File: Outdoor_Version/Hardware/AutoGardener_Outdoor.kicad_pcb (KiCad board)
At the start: 2 copper layers, 22 x 30 mm, 25 parts, among them J1 SWO, J2 Header_1x3, J3 Header_1x3, J4 Header_1x2, Q1 FDN308P, Q2 IRLML6346TRPBF, U1 STM32L031K6T6, U2 AP2204RB-3.3TRG1

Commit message: Started a new kicad project.
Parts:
- moved R2 7.25 mm to (222.0, 100.0), turned to 0 degrees
- moved LD13 4.78 mm to (226.0, 100.0), turned to 180 degrees
- moved SB2 3.06 mm to (225.8, 85.6)
- moved BAT1 3.00 mm to (217.0, 109.0), turned to 270 degrees
- moved C3 2.46 mm to (227.0, 97.0)
- moved LD3 1.82 mm to (226.0, 104.0), turned to 180 degrees
- moved C1 1.26 mm to (215.6, 89.2), turned to 180 degrees
- moved R3 1.12 mm to (222.0, 102.0)
- moved Q2 0.79 mm to (222.0, 105.0)
- moved C2 0.72 mm to (215.6, 92.4), turned to 180 degrees
- moved SB1 0.15 mm to (219.5, 85.6)
- turned C4 to 180 degrees
- turned C5 to 180 degrees
- turned C6 to 180 degrees
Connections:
- J2 pad 1: /UART_TX -> /UART_RX
- J2 pad 2: /UART_RX -> /UART_TX
- U1 pad 10: Net-(U1-Pad10) -> /BAT_LO
- U1 pad 15: /SENS_ENA -> Net-(U1-Pad15)
- U1 pad 18: /BAT_LO -> Net-(U1-Pad18)
- U1 pad 25: Net-(U1-Pad25) -> /SENS_ENA
- U1 pad 27: /OUT1 -> Net-(U1-Pad27)
- U1 pad 9: Net-(U1-Pad9) -> /OUT1
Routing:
- net VCC: track 0.00 -> 51.5 mm, vias 0 -> 3
- net /NRST: track 0.00 -> 23.4 mm, vias 0 -> 2
- net /UART_TX: track 0.00 -> 16.7 mm
- net /UART_RX: track 0.00 -> 15.1 mm
- net /ADC_SOIL1: track 0.00 -> 13.9 mm, vias 0 -> 1
- net /SENS_ENA: track 0.00 -> 12.7 mm, vias 0 -> 2
- net +5V: track 0.00 -> 11.5 mm
- net /SWDIO: track 0.00 -> 10.2 mm
- net /OUT1: track 0.00 -> 9.30 mm
- net /SWCLK: track 0.00 -> 6.29 mm
- net VDDA: track 0.00 -> 5.85 mm
- net /BAT_LO: track 0.00 -> 4.12 mm
- net Net-(J4-Pad2): track 0.00 -> 4.12 mm
- net Net-(LD3-Pad2): track 0.00 -> 3.62 mm
- net GND: track 0.00 -> 2.88 mm, vias 0 -> 23
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- added copper zone on F.Cu, net GND
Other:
- board text added: "+"
- board text added: "-"
- board text added: "AUTOGARDENER OUTDOOR v1"
- board text added: "BAT"
- board text added: "G"
- board text added: "RX TX GND"
- board text added: "S"
- board text added: "SOIL SENSOR"
- board text added: "SWO"
- board text added: "UART"
- board text added: "V"
- board text added: "VALVE"

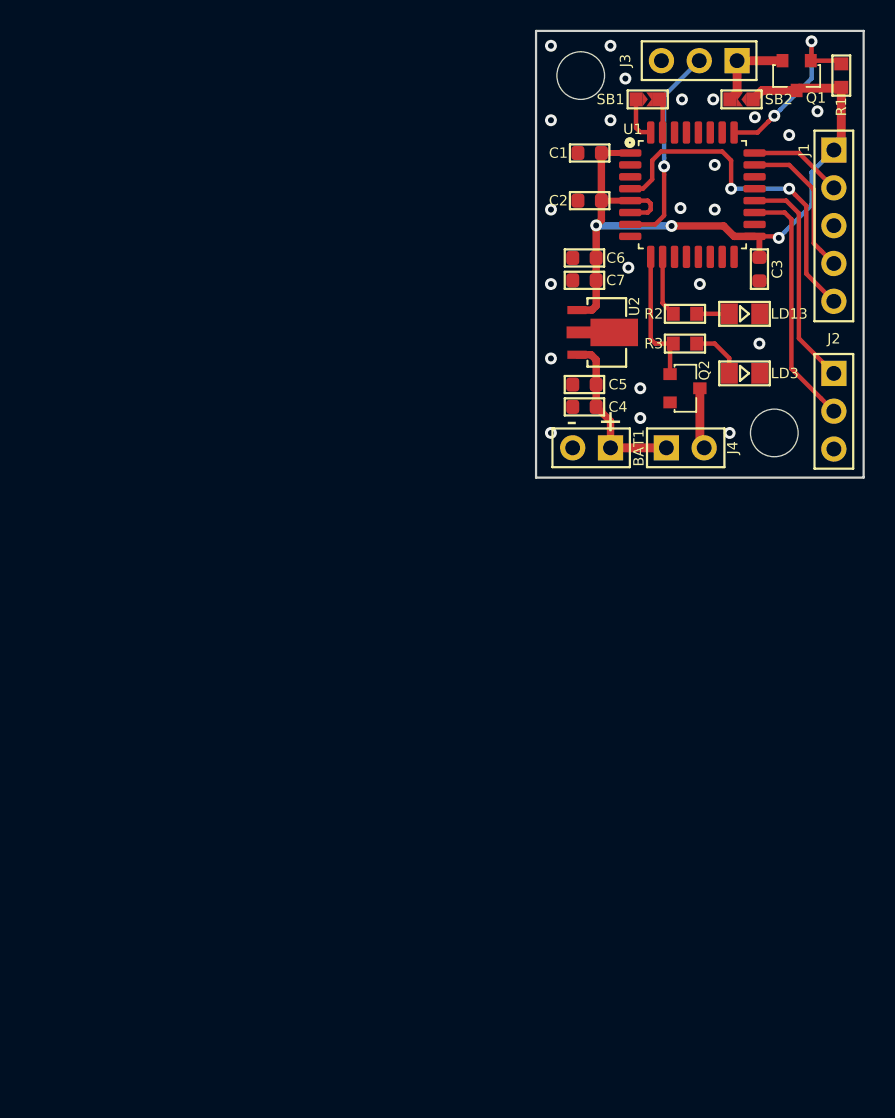
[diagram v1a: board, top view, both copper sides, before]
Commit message: Finished the design of the outdoor version of the gardener. Generated Gerbers.
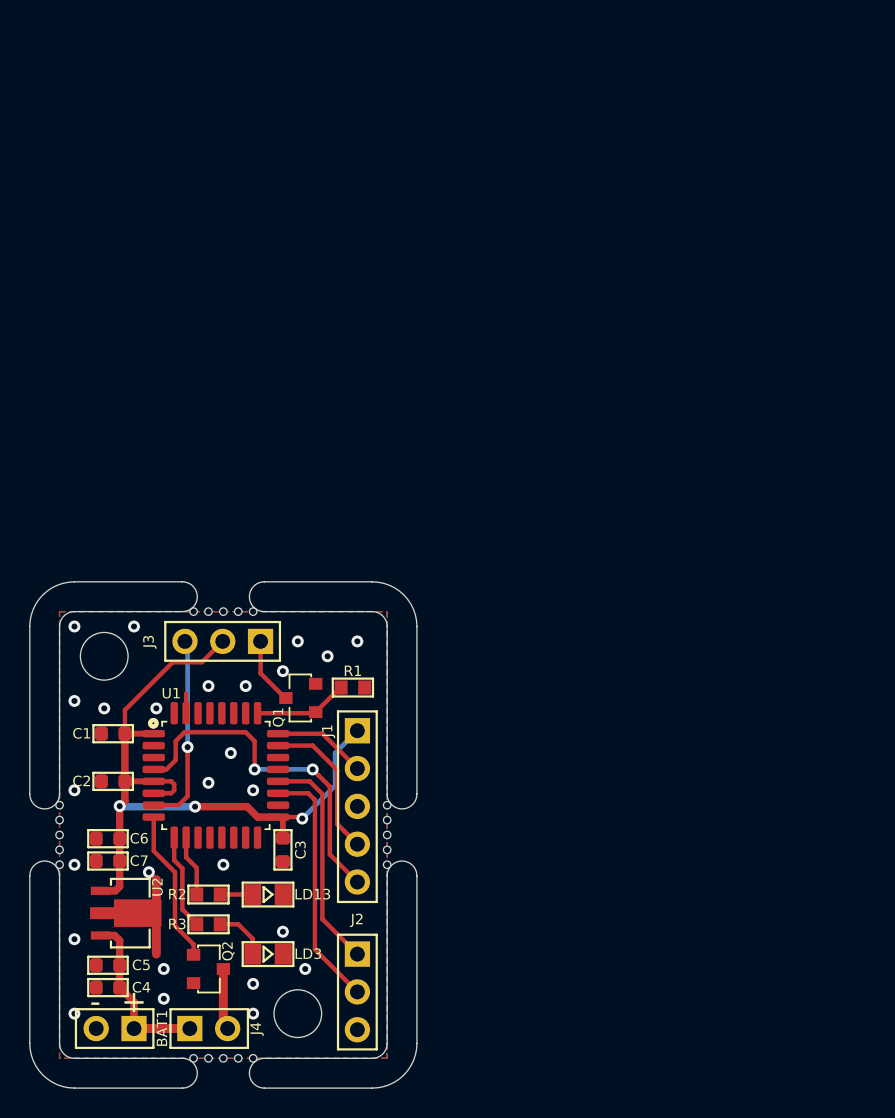
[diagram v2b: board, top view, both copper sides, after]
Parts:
- removed SB1, SB2: SolderBridge, MRS_Connectors:SB0603
- added H111: Mr_Gardener_Logo_Small, Logos:mrg_gardener_08mm, B.Cu at (195.0, 139.0)
- added H3: Break_away_tab, MRS_Mechanical:Breakaway_tab_holes, F.Cu at (191.0, 120.0)
- added H4: Break_away_tab, MRS_Mechanical:Breakaway_tab_holes, F.Cu at (191.0, 150.0)
- added H5: Break_away_tab, MRS_Mechanical:Breakaway_tab_holes, F.Cu at (202.0, 135.0)
- added H6: Break_away_tab, MRS_Mechanical:Breakaway_tab_holes, F.Cu at (180.0, 135.0)
- Q1: value FDN308P -> 2N7002P.215
- Q2: value IRLML6346TRPBF -> 2N7002P.215
- moved Q1 53.4 mm to (196.2, 125.8), turned to 180 degrees
- moved R1 52.6 mm to (199.7, 125.1), turned to 0 degrees
- moved BAT1 50.4 mm to (185.0, 148.0)
- moved C2 50.4 mm to (183.6, 131.4)
- moved C3 50.4 mm to (195.0, 136.0)
- moved C4 50.4 mm to (183.2, 145.2)
- moved C5 50.4 mm to (183.2, 143.8)
- moved C6 50.4 mm to (183.2, 135.2)
- moved C7 50.4 mm to (183.2, 136.8)
- moved H1 50.4 mm to (183.0, 123.0)
- moved H2 50.4 mm to (196.0, 147.0)
- moved J1 50.4 mm to (200.0, 128.0)
- moved J2 50.4 mm to (200.0, 143.0)
- moved J3 50.4 mm to (193.5, 122.0)
- moved J4 50.4 mm to (188.8, 148.0)
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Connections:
- J3 pad 1: VDDA -> Net-(J3-Pad1)
- J3 pad 2: /ADC_SOIL1 -> VCC
- J3 pad 3: GND -> /ADC_SOIL1
- Q1 pad 2: VDDA -> GND
- Q1 pad 3: VCC -> Net-(J3-Pad1)
- R1 pad 1: VCC -> /SENS_ENA
- R1 pad 2: /SENS_ENA -> GND
- R3 pad 1: /OUT1 -> /LED1
- U1 pad 31: Net-(SB1-Pad2) -> GND
- U1 pad 8: Net-(U1-Pad8) -> /OUT1
- U1 pad 9: /OUT1 -> /LED1
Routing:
- net /LED1: track 0.00 -> 6.75 mm
- net /SENS_ENA: track 12.7 -> 6.33 mm, vias 2 -> 0
- net VDDA: track 5.85 -> 0.00 mm
- net GND: track 2.88 -> 8.11 mm, vias 23 -> 26
- net Net-(J3-Pad1): track 0.00 -> 4.53 mm
- net Net-(SB1-Pad2): track 2.16 -> 0.00 mm
- net /OUT1: track 9.30 -> 10.4 mm
- net /ADC_SOIL1: track 13.9 -> 13.0 mm
- net VCC: track 51.5 -> 50.9 mm
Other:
- board size 22 x 30 mm -> 26 x 34 mm
- board text added: "A"
- board text added: "Mr. Gardener Jr."
- board text added: "rev 1"
- board text removed: "AUTOGARDENER OUTDOOR v1"
- board text removed: "S"

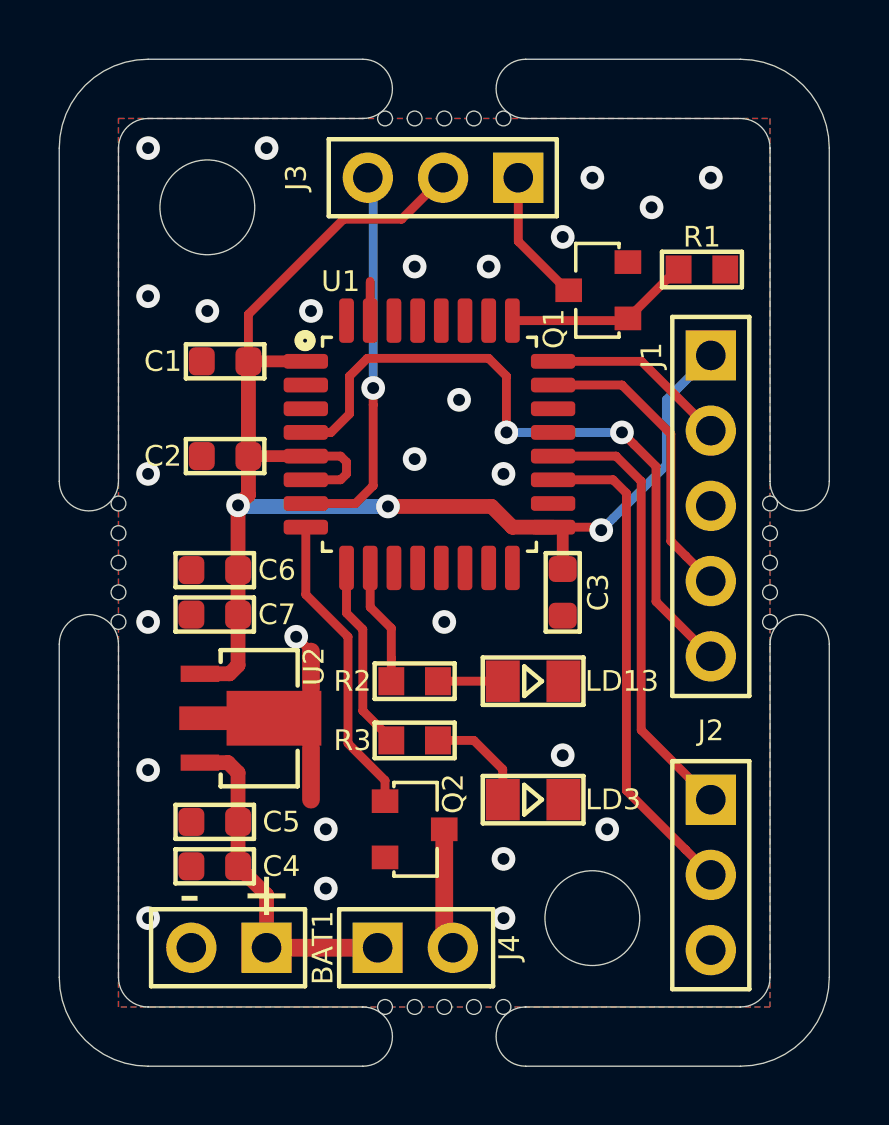
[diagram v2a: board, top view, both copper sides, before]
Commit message: Added some mechanical details into the PCB document.
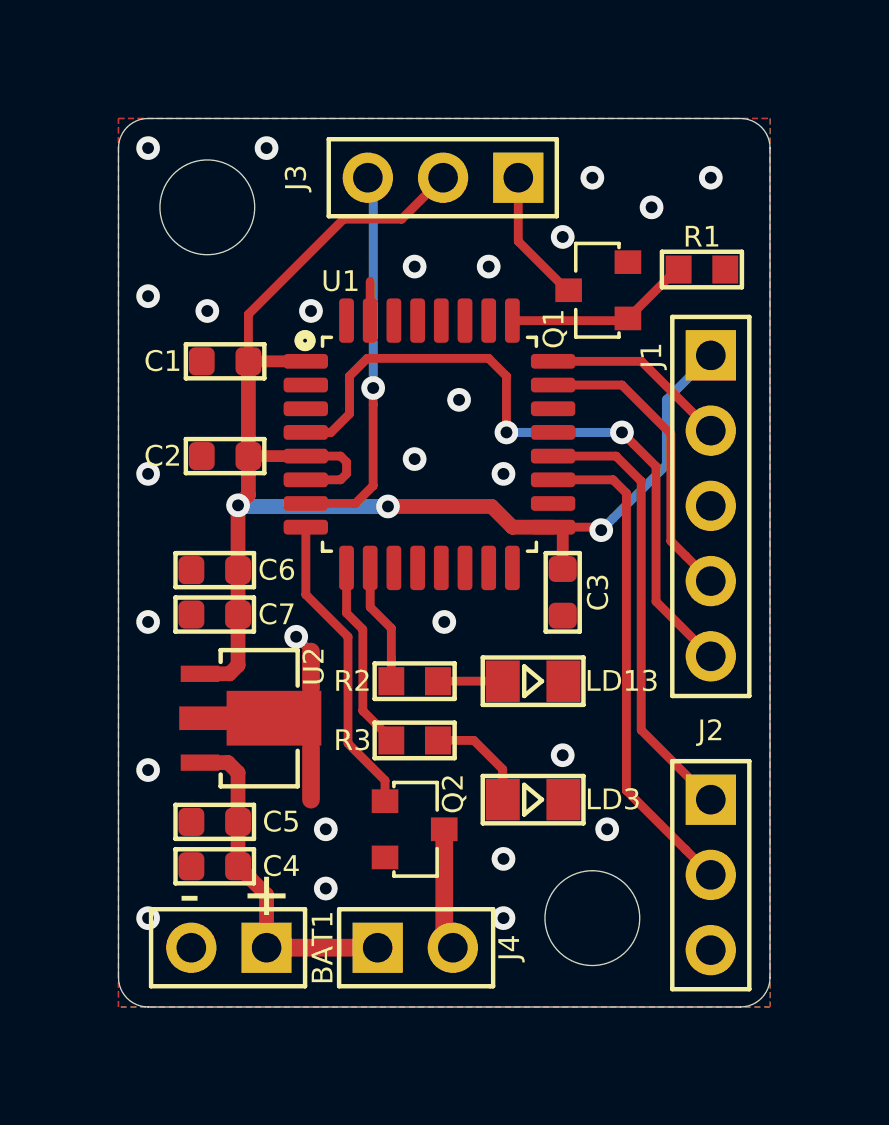
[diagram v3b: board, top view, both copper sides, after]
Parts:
- removed H3, H4, H5, H6: Break_away_tab, MRS_Mechanical:Breakaway_tab_holes
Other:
- board size 26 x 34 mm -> 22 x 30 mm
